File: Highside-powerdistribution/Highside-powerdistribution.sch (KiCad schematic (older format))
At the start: 13 parts

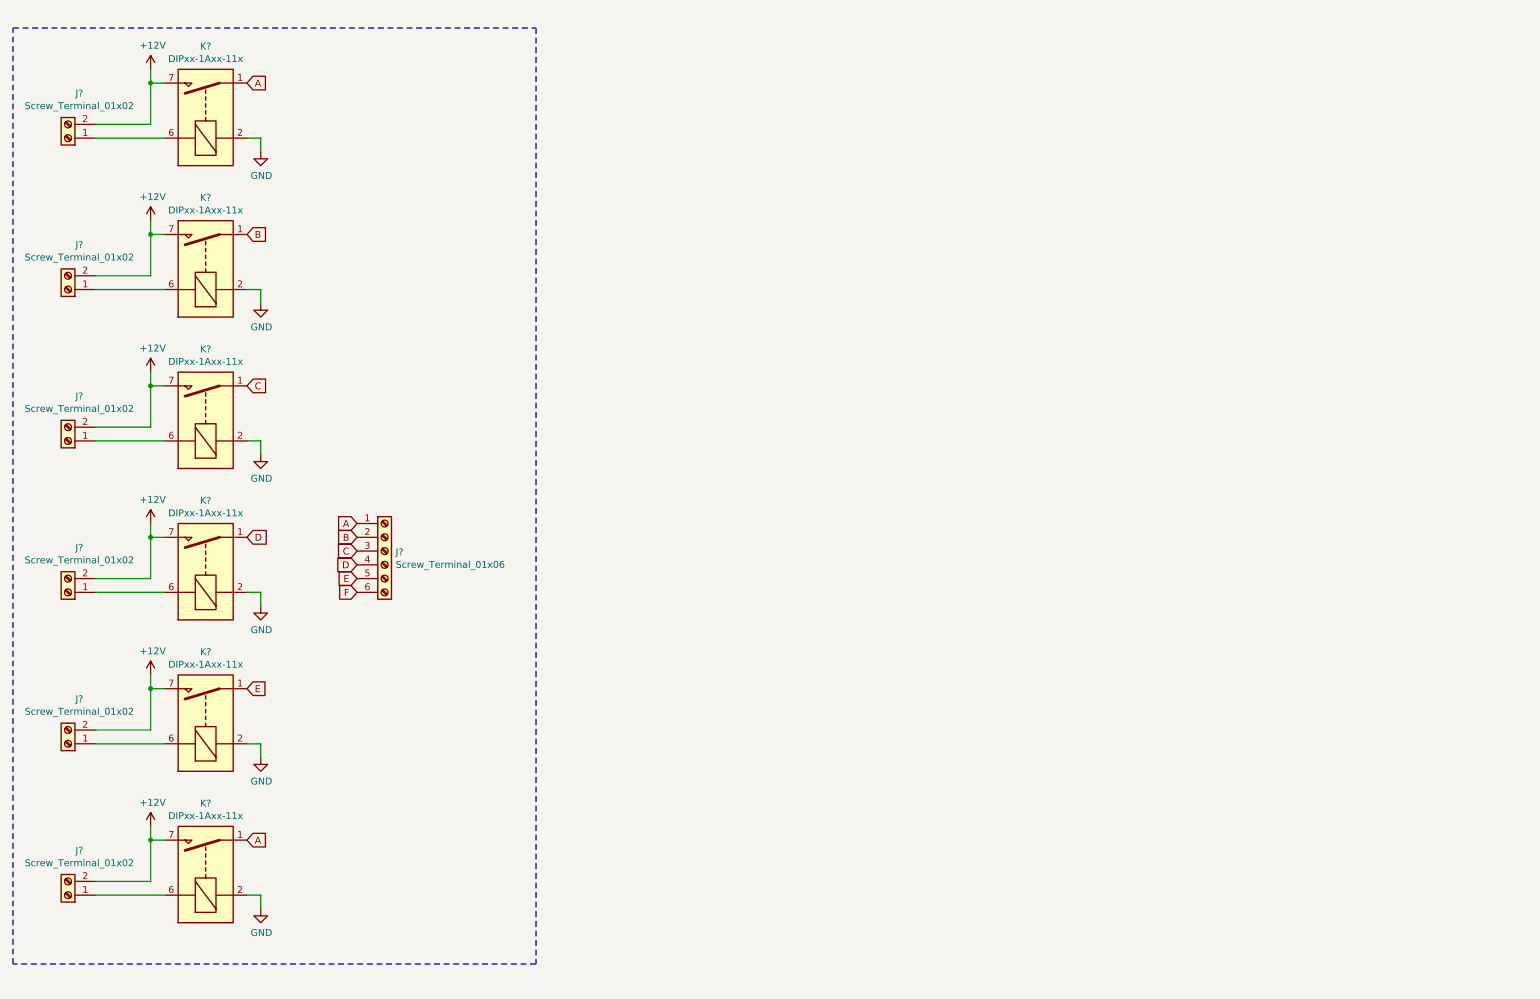
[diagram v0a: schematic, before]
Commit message: Assign footprint
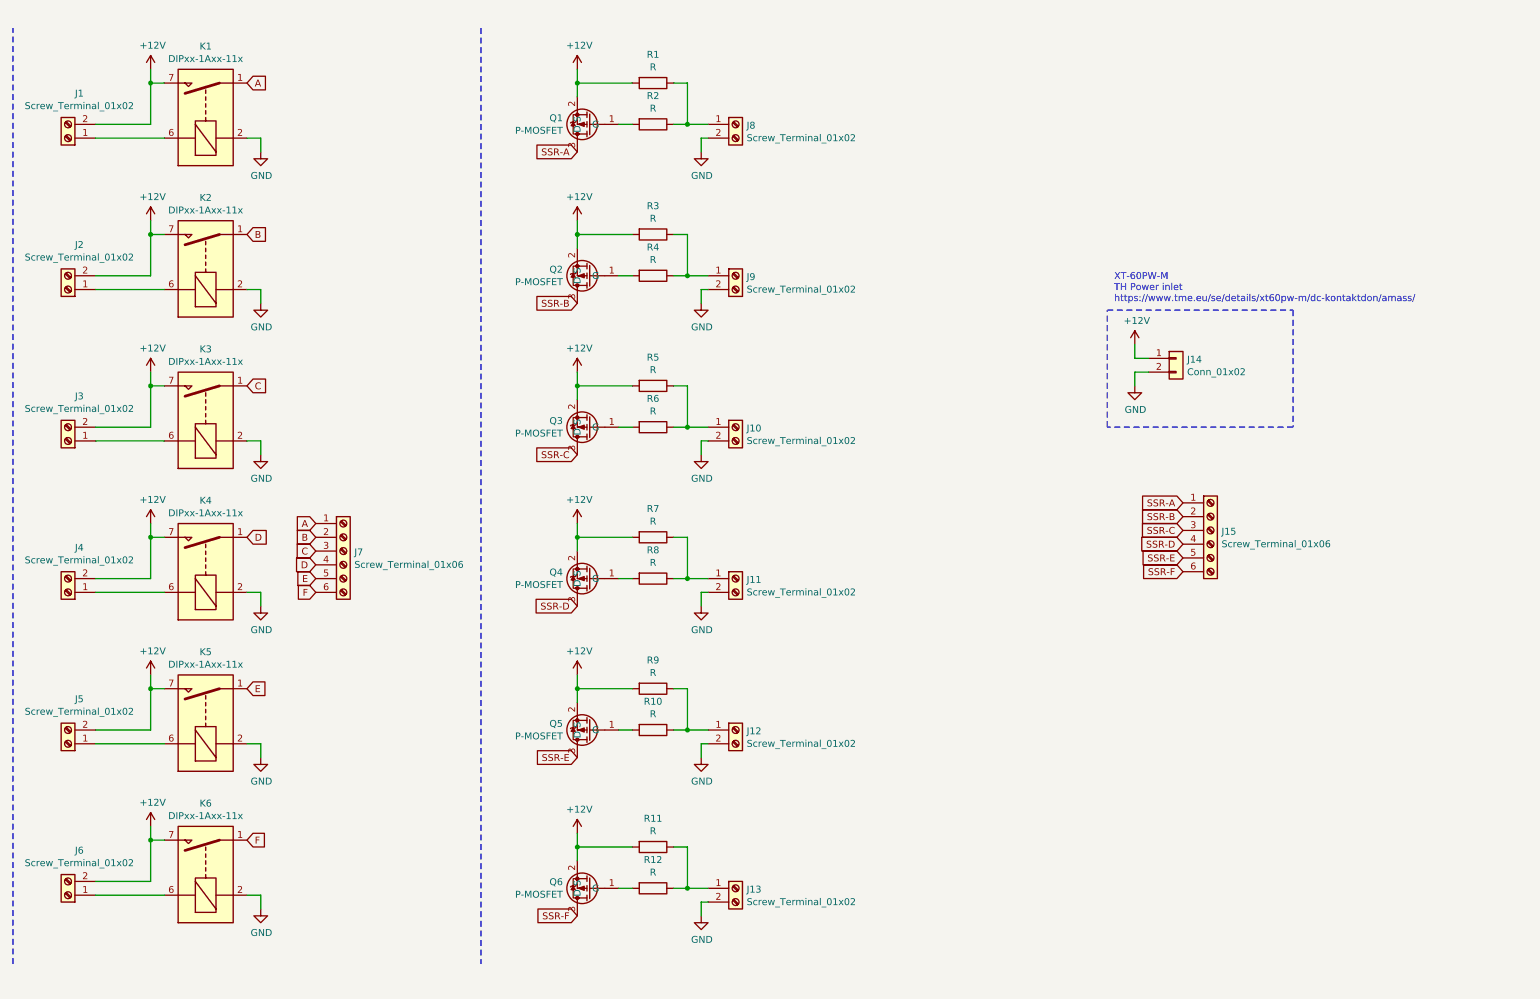
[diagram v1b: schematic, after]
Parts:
- added J10, J11, J12, J13, J8, J9: Screw_Terminal_01x02, Highside-powerdistribution:PTSA 1,5 2-3,5-Z, symbol Connector:Screw_Terminal_01x02
- added J14: Conn_01x02, Highside-powerdistribution:XT60PW-F, symbol Connector_Generic:Conn_01x02
- added J15: Screw_Terminal_01x06, Highside-powerdistribution:ETB11060B000Z, symbol Connector:Screw_Terminal_01x06
- added Q1, Q2, Q3, Q4, Q5, Q6: P-MOSFET, Highside-powerdistribution:AOI403, symbol Highside-powerdistribution:P-MOSFET
- added R1, R10, R11, R12, R2, R3, R4, R5, R6, R7, R8, R9: R, Resistor_SMD:R_0603_1608Metric_Pad1.05x0.95mm_HandSolder, symbol Device:R
- J1, J2, J3, J4, J5, J6: renamed from J?; footprint (none) -> Highside-powerdistribution:PTSA 1,5 2-3,5-Z
- gave numbers to parts that had none: 7
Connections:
- net +12V: now also J14.1 (Pin_1), Q1.2 (S), Q2.2 (S), Q3.2 (S), Q4.2 (S), Q5.2 (S), Q6.2 (S), R1.2, R11.2, R3.2, R5.2, R7.2, R9.2
- net A: no longer K6.1, K6.14
- net F: now also K6.1, K6.14
- net GND: now also J10.2 (Pin_2), J11.2 (Pin_2), J12.2 (Pin_2), J13.2 (Pin_2), J14.2 (Pin_2), J8.2 (Pin_2), J9.2 (Pin_2)
- new net: Q1.1 (G), R2.2
- new net: Q2.1 (G), R4.2
- new net: Q3.1 (G), R6.2
- new net: Q4.1 (G), R8.2
- new net: Q5.1 (G), R10.2
- new net: J8.1 (Pin_1), R1.1, R2.1
- new net: J13.1 (Pin_1), R11.1, R12.1
- new net: Q6.1 (G), R12.2
- new net: J9.1 (Pin_1), R3.1, R4.1
- new net: J10.1 (Pin_1), R5.1, R6.1
- new net: J11.1 (Pin_1), R7.1, R8.1
- new net: J12.1 (Pin_1), R10.1, R9.1
- new net SSR-A: J15.1 (Pin_1), Q1.3 (D)
- new net SSR-B: J15.2 (Pin_2), Q2.3 (D)
- new net SSR-C: J15.3 (Pin_3), Q3.3 (D)
- new net SSR-D: J15.4 (Pin_4), Q4.3 (D)
- new net SSR-E: J15.5 (Pin_5), Q5.3 (D)
- new net SSR-F: J15.6 (Pin_6), Q6.3 (D)
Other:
- note added: "XT-60PW-M \nTH Power inlet\nhttps://www.tme.eu/se/details/xt60pw-m/dc-kontaktdon/amass/"
- moved on the sheet: J7

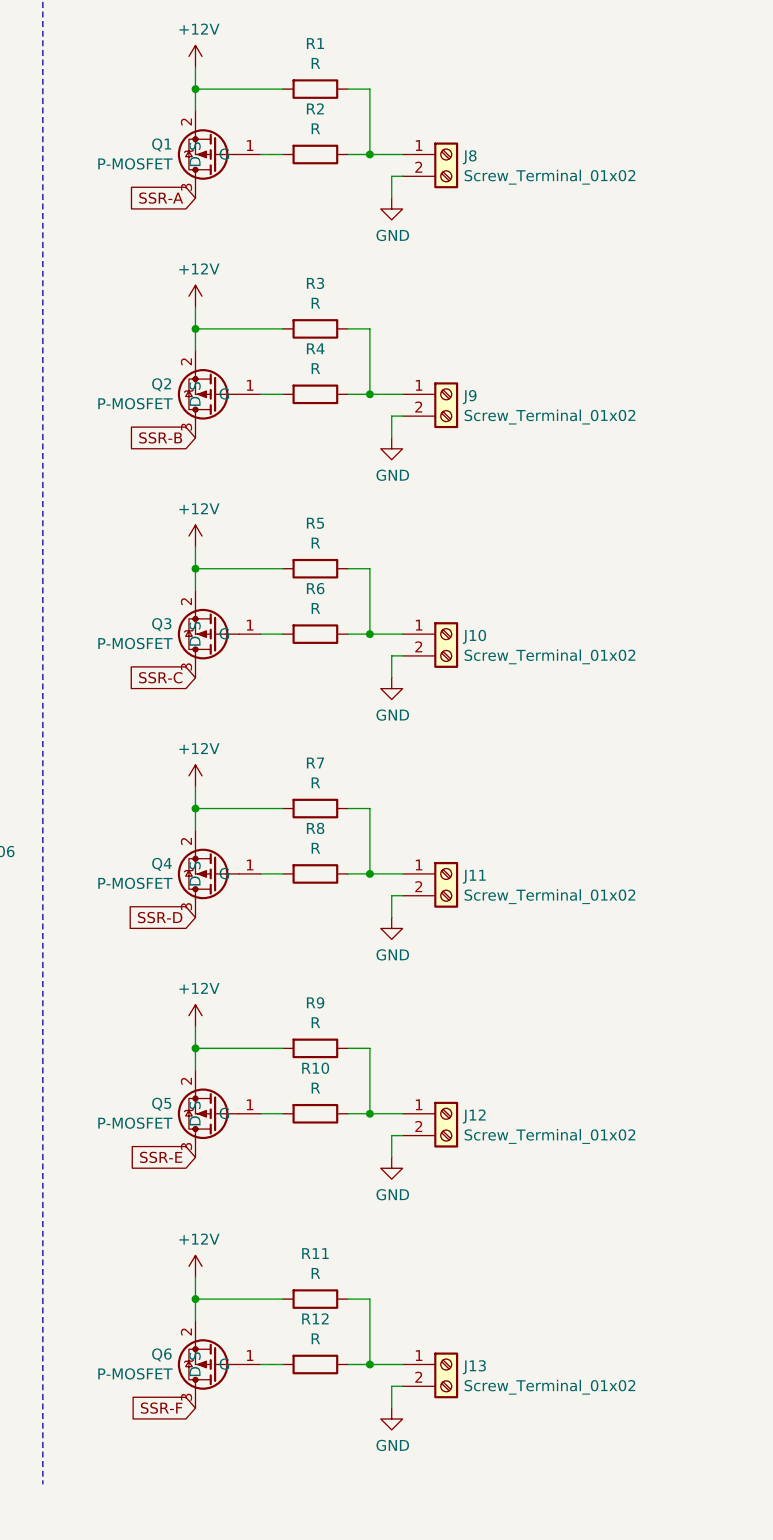
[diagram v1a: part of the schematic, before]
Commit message: Added mounting holes.
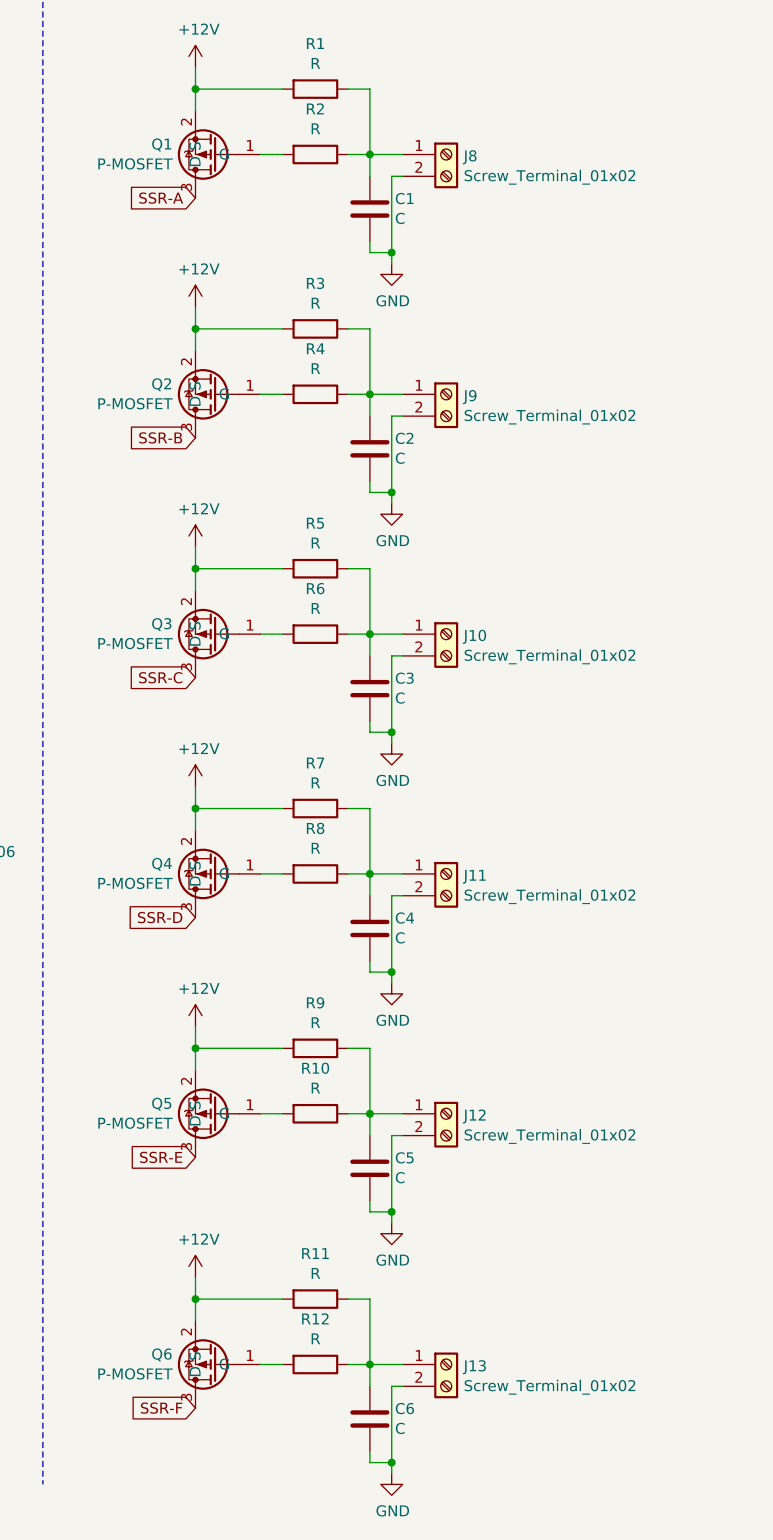
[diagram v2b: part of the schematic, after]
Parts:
- added C1, C2, C3, C4, C5, C6: C, Capacitor_SMD:C_0603_1608Metric_Pad1.05x0.95mm_HandSolder, symbol Device:C
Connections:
- net GND: now also C1.2, C2.2, C3.2, C4.2, C5.2, C6.2
- net at J8.1 (Pin_1), R1.1, R2.1: now also C1.1
- net at J13.1 (Pin_1), R11.1, R12.1: now also C6.1
- net at J9.1 (Pin_1), R3.1, R4.1: now also C2.1
- net at J10.1 (Pin_1), R5.1, R6.1: now also C3.1
- net at J11.1 (Pin_1), R7.1, R8.1: now also C4.1
- net at J12.1 (Pin_1), R10.1, R9.1: now also C5.1
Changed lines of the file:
@@
 L power:GND #PWR0114
 U 1 1 5DD1DB0E
-P 5600 1700
-F 0 "#PWR0114" H 5600 1450 50  0001 C CNN
-F 1 "GND" H 5605 1527 50  0000 C CNN
-F 2 "" H 5600 1700 50  0001 C CNN
-F 3 "" H 5600 1700 50  0001 C CNN
-	1    5600 1700
-	1    0    0    -1
-$EndComp
-Wire Wire Line
-	5600 1700 5600 1600
+P 5600 2000
+F 0 "#PWR0114" H 5600 1750 50  0001 C CNN
+F 1 "GND" H 5605 1827 50  0000 C CNN
+F 2 "" H 5600 2000 50  0001 C CNN
+F 3 "" H 5600 2000 50  0001 C CNN
+	1    5600 2000
+	1    0    0    -1
+$EndComp
 Wire Wire Line
 	5600 1600 5650 1600
@@
 L power:GND #PWR0116
 U 1 1 5DD3FDE7
-P 5600 2800
-F 0 "#PWR0116" H 5600 2550 50  0001 C CNN
-F 1 "GND" H 5605 2627 50  0000 C CNN
-F 2 "" H 5600 2800 50  0001 C CNN
-F 3 "" H 5600 2800 50  0001 C CNN
-	1    5600 2800
-	1    0    0    -1
-$EndComp
-Wire Wire Line
-	5600 2800 5600 2700
+P 5600 3100
+F 0 "#PWR0116" H 5600 2850 50  0001 C CNN
+F 1 "GND" H 5605 2927 50  0000 C CNN
+F 2 "" H 5600 3100 50  0001 C CNN
+F 3 "" H 5600 3100 50  0001 C CNN
+	1    5600 3100
+	1    0    0    -1
+$EndComp
 Wire Wire Line
 	5600 2700 5650 2700
@@
 L power:GND #PWR0118
 U 1 1 5DD4BB6F
-P 5600 3900
-F 0 "#PWR0118" H 5600 3650 50  0001 C CNN
-F 1 "GND" H 5605 3727 50  0000 C CNN
-F 2 "" H 5600 3900 50  0001 C CNN
-F 3 "" H 5600 3900 50  0001 C CNN
-	1    5600 3900
-	1    0    0    -1
-$EndComp
-Wire Wire Line
-	5600 3900 5600 3800
+P 5600 4200
+F 0 "#PWR0118" H 5600 3950 50  0001 C CNN
+F 1 "GND" H 5605 4027 50  0000 C CNN
+F 2 "" H 5600 4200 50  0001 C CNN
+F 3 "" H 5600 4200 50  0001 C CNN
+	1    5600 4200
+	1    0    0    -1
+$EndComp
 Wire Wire Line
 	5600 3800 5650 3800
@@
 L power:GND #PWR0120
 U 1 1 5DD4ECB7
-P 5600 5000
-F 0 "#PWR0120" H 5600 4750 50  0001 C CNN
-F 1 "GND" H 5605 4827 50  0000 C CNN
-F 2 "" H 5600 5000 50  0001 C CNN
-F 3 "" H 5600 5000 50  0001 C CNN
-	1    5600 5000
-	1    0    0    -1
-$EndComp
-Wire Wire Line
-	5600 5000 5600 4900
+P 5600 5300
+F 0 "#PWR0120" H 5600 5050 50  0001 C CNN
+F 1 "GND" H 5605 5127 50  0000 C CNN
+F 2 "" H 5600 5300 50  0001 C CNN
+F 3 "" H 5600 5300 50  0001 C CNN
+	1    5600 5300
+	1    0    0    -1
+$EndComp
 Wire Wire Line
 	5600 4900 5650 4900
@@
 L power:GND #PWR0122
 U 1 1 5DD521C6
-P 5600 6100
-F 0 "#PWR0122" H 5600 5850 50  0001 C CNN
-F 1 "GND" H 5605 5927 50  0000 C CNN
-F 2 "" H 5600 6100 50  0001 C CNN
-F 3 "" H 5600 6100 50  0001 C CNN
-	1    5600 6100
-	1    0    0    -1
-$EndComp
-Wire Wire Line
-	5600 6100 5600 6000
+P 5600 6400
+F 0 "#PWR0122" H 5600 6150 50  0001 C CNN
+F 1 "GND" H 5605 6227 50  0000 C CNN
+F 2 "" H 5600 6400 50  0001 C CNN
+F 3 "" H 5600 6400 50  0001 C CNN
+	1    5600 6400
+	1    0    0    -1
+$EndComp
 Wire Wire Line
 	5600 6000 5650 6000
@@
 	1    0    0    -1
 $EndComp
-$Comp
-L power:GND #PWR0126
-U 1 1 5DD24805
-P 5600 7250
-F 0 "#PWR0126" H 5600 7000 50  0001 C CNN
-F 1 "GND" H 5605 7077 50  0000 C CNN
-F 2 "" H 5600 7250 50  0001 C CNN
-F 3 "" H 5600 7250 50  0001 C CNN
-	1    5600 7250
-	1    0    0    -1
-$EndComp
-Wire Wire Line
-	5600 7250 5600 7150
 Wire Wire Line
 	5600 7150 5650 7150
@@
 Text GLabel 9100 4750 0    50   Input ~ 0
 SSR-F
+$Comp
+L Device:C C1
+U 1 1 5DD687AC
+P 5500 1750
+F 0 "C1" H 5615 1796 50  0000 L CNN
+F 1 "C" H 5615 1705 50  0000 L CNN
+F 2 "Capacitor_SMD:C_0603_1608Metric_Pad1.05x0.95mm_HandSolder" H 5538 1600 50  0001 C CNN
+F 3 "~" H 5500 1750 50  0001 C CNN
+	1    5500 1750
+	1    0    0    -1
+$EndComp
+$Comp
+L Device:C C2
+U 1 1 5DD68F04
+P 5500 2850
+F 0 "C2" H 5615 2896 50  0000 L CNN
+F 1 "C" H 5615 2805 50  0000 L CNN
+F 2 "Capacitor_SMD:C_0603_1608Metric_Pad1.05x0.95mm_HandSolder" H 5538 2700 50  0001 C CNN
+F 3 "~" H 5500 2850 50  0001 C CNN
+	1    5500 2850
+	1    0    0    -1
+$EndComp
+$Comp
+L Device:C C3
+U 1 1 5DD69507
+P 5500 3950
+F 0 "C3" H 5615 3996 50  0000 L CNN
+F 1 "C" H 5615 3905 50  0000 L CNN
+F 2 "Capacitor_SMD:C_0603_1608Metric_Pad1.05x0.95mm_HandSolder" H 5538 3800 50  0001 C CNN
+F 3 "~" H 5500 3950 50  0001 C CNN
+	1    5500 3950
+	1    0    0    -1
+$EndComp
+$Comp
+L Device:C C4
+U 1 1 5DD6A05D
+P 5500 5050
+F 0 "C4" H 5615 5096 50  0000 L CNN
+F 1 "C" H 5615 5005 50  0000 L CNN
+F 2 "Capacitor_SMD:C_0603_1608Metric_Pad1.05x0.95mm_HandSolder" H 5538 4900 50  0001 C CNN
+F 3 "~" H 5500 5050 50  0001 C CNN
+	1    5500 5050
+	1    0    0    -1
+$EndComp
+$Comp
+L Device:C C5
+U 1 1 5DD6AA38
+P 5500 6150
+F 0 "C5" H 5615 6196 50  0000 L CNN
+F 1 "C" H 5615 6105 50  0000 L CNN
+F 2 "Capacitor_SMD:C_0603_1608Metric_Pad1.05x0.95mm_HandSolder" H 5538 6000 50  0001 C CNN
+F 3 "~" H 5500 6150 50  0001 C CNN
+	1    5500 6150
+	1    0    0    -1
+$EndComp
+$Comp
+L Device:C C6
+U 1 1 5DD6B462
+P 5500 7300
+F 0 "C6" H 5615 7346 50  0000 L CNN
+F 1 "C" H 5615 7255 50  0000 L CNN
+F 2 "Capacitor_SMD:C_0603_1608Metric_Pad1.05x0.95mm_HandSolder" H 5538 7150 50  0001 C CNN
+F 3 "~" H 5500 7300 50  0001 C CNN
+	1    5500 7300
+	1    0    0    -1
+$EndComp
+$Comp
+L power:GND #PWR0126
+U 1 1 5DD24805
+P 5600 7550
+F 0 "#PWR0126" H 5600 7300 50  0001 C CNN
+F 1 "GND" H 5605 7377 50  0000 C CNN
+F 2 "" H 5600 7550 50  0001 C CNN
+F 3 "" H 5600 7550 50  0001 C CNN
+	1    5600 7550
+	1    0    0    -1
+$EndComp
+Wire Wire Line
+	5500 1600 5500 1500
+Wire Wire Line
+	5600 1600 5600 1950
+Wire Wire Line
+	5500 1900 5500 1950
+Wire Wire Line
+	5500 1950 5600 1950
+Connection ~ 5600 1950
+Wire Wire Line
+	5600 1950 5600 2000
+Wire Wire Line
+	5500 2600 5500 2700
+Wire Wire Line
+	5600 2700 5600 3050
+Wire Wire Line
+	5500 3000 5500 3050
+Wire Wire Line
+	5500 3050 5600 3050
+Connection ~ 5600 3050
+Wire Wire Line
+	5600 3050 5600 3100
+Wire Wire Line
+	5600 3800 5600 4150
+Wire Wire Line
+	5500 3800 5500 3700
+Wire Wire Line
+	5500 4100 5500 4150
+Wire Wire Line
+	5500 4150 5600 4150
+Connection ~ 5600 4150
+Wire Wire Line
+	5600 4150 5600 4200
+Wire Wire Line
+	5500 4800 5500 4900
+Wire Wire Line
+	5600 4900 5600 5250
+Wire Wire Line
+	5500 5200 5500 5250
+Wire Wire Line
+	5500 5250 5600 5250
+Connection ~ 5600 5250
+Wire Wire Line
+	5600 5250 5600 5300
+Wire Wire Line
+	5500 5900 5500 6000
+Wire Wire Line
+	5600 6000 5600 6350
+Wire Wire Line
+	5500 6300 5500 6350
+Wire Wire Line
+	5500 6350 5600 6350
+Connection ~ 5600 6350
+Wire Wire Line
+	5600 6350 5600 6400
+Wire Wire Line
+	5600 7150 5600 7500
+Wire Wire Line
+	5500 7150 5500 7050
+Wire Wire Line
+	5500 7450 5500 7500
+Wire Wire Line
+	5500 7500 5600 7500
+Connection ~ 5600 7500
+Wire Wire Line
+	5600 7500 5600 7550
 $EndSCHEMATC
